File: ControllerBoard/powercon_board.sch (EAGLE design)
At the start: 49 parts, among them CN1 POWER_IF, CN2 PICkit_IF, CN3 ROTARY_ENCODER, CN4 UART_IF, CN5 POWER_IF_FOR_ESP, Q1 2SC1815, SW1 10-XX, SW2 10-XX, SW3 10-XX, SW4 10-XX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

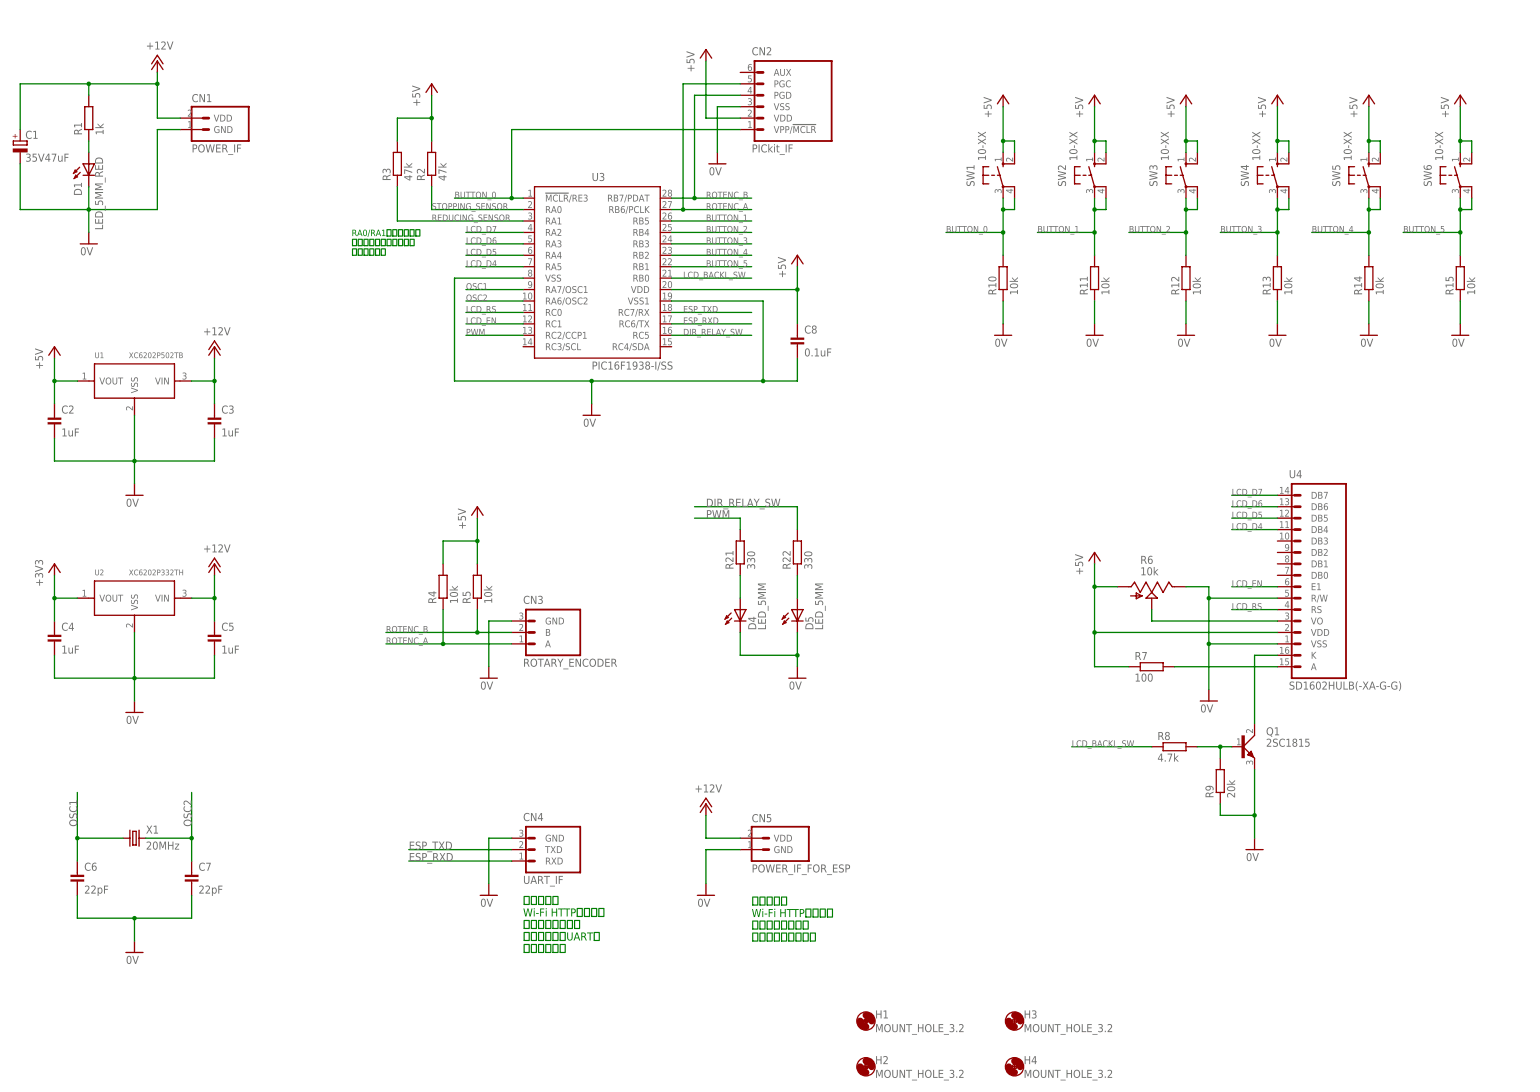
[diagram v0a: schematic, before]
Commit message: MODE_SELECT端子を新設
・PICのファームウェアを共通化する目的
・MODE_SELECT=LOWの場合は親機（パワーコントローラー部）
・MODE_SELECT=HIGHの場合は子機（リモコン部）
・ディレクトリー名を EAGLE —> ControllerBoardに改称
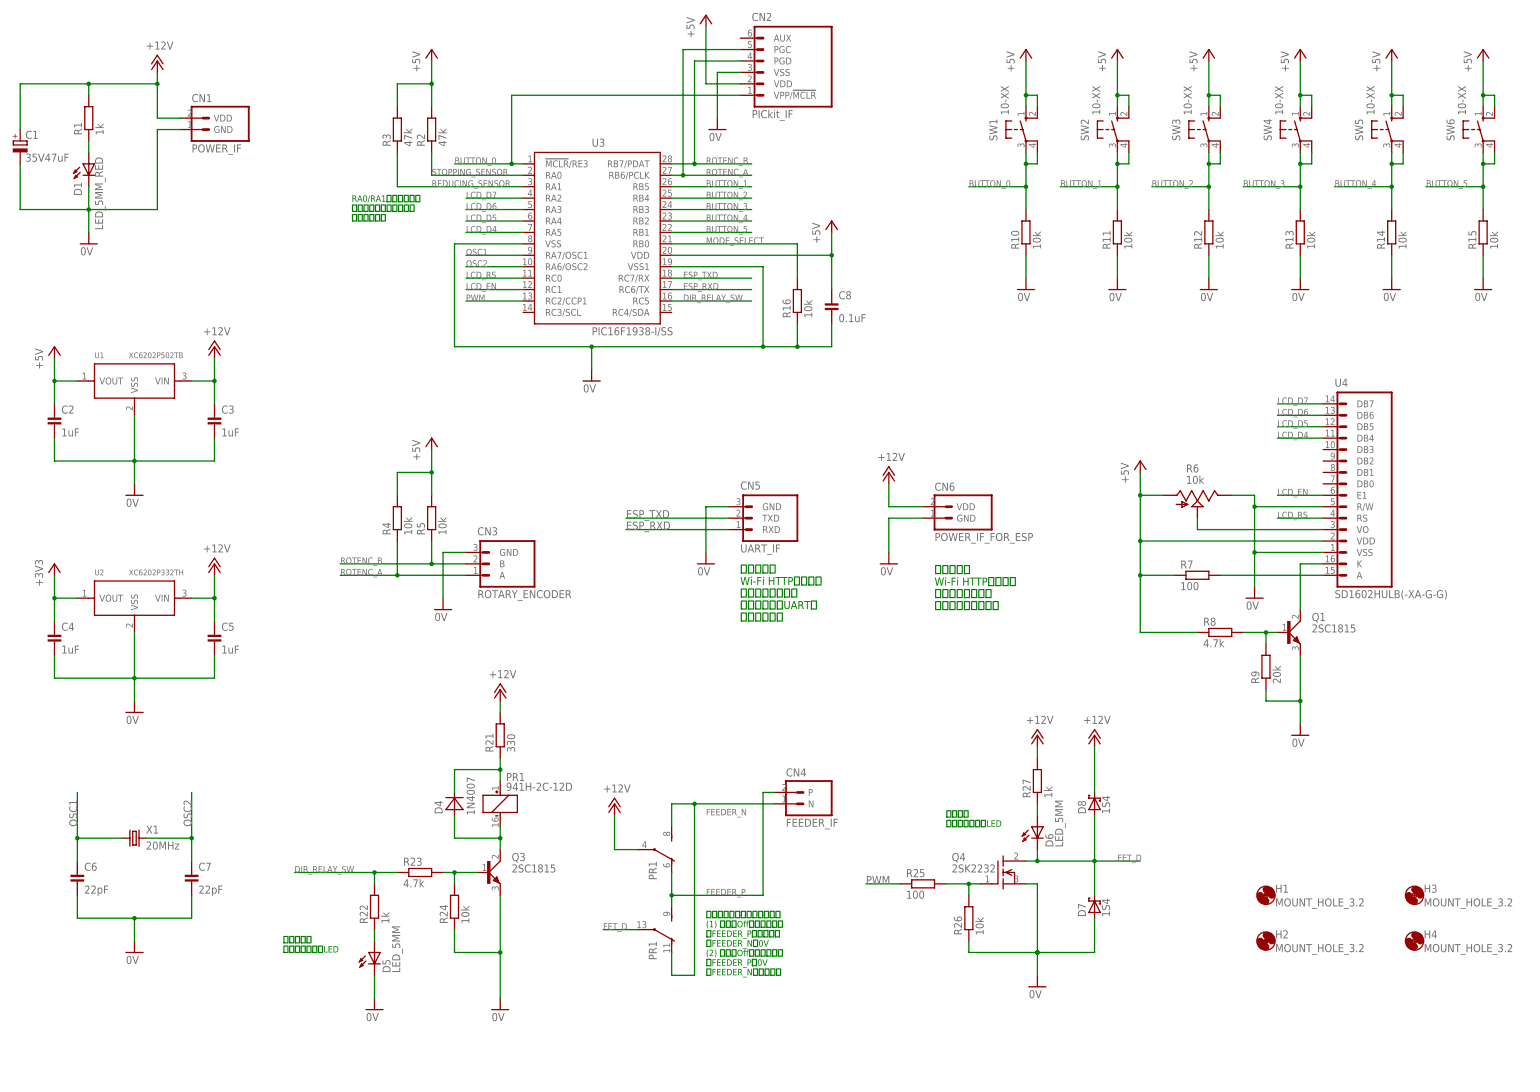
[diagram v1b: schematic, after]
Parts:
- added CN6: POWER_IF_FOR_ESP, PartsForProto:POWER_IF
- added D6: LED_5MM, Parts:LED_5MM
- added D7, D8: 1S4, Parts:1S4
- added PR1: 941H-2C-12D, Parts:941H-2C-12D
- added Q3: 2SC1815, Parts:2SC1815
- added Q4: 2SK2232, Parts:2SK2232
- added R16, R24, R26: 10k, Parts:RESISTOR_300MIL
- added R23: 4.7k, Parts:RESISTOR_300MIL
- added R25: 100, Parts:RESISTOR_300MIL
- added R27: 1k, Parts:RESISTOR_300MIL
- CN4: value UART_IF -> FEEDER_IF; device PartsForProto:UART_IF -> PartsForProto:FEEDER_IF
- CN5: value POWER_IF_FOR_ESP -> UART_IF; device PartsForProto:POWER_IF -> PartsForProto:UART_IF
- D4: value LED_5MM -> 1N4007; device Parts:LED_5MM -> Parts:1N4007
- R22: value 330 -> 1k
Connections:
- removed net LCD_BACKL_SW: R8.1, U3.RB0
- new net +3V3: C4.1, U2.VOUT
- new net FEEDER_N: CN4.N, PR12.S, PR13.O
- new net FEEDER_P: CN4.P, PR12.O, PR13.S
- new net FET_D: D6.C, D7.C, D8.A, PR13.P, Q4.D
- new net MODE_SELECT: R16.2, U3.RB0
- new net N$13: D4.C, PR11.+, R21.1
- new net N$14: Q3.B, R23.2, R24.2
- new net N$15: D4.A, PR11.-, Q3.C
- new net N$3: Q4.G, R25.2, R26.2
- net +12V: now also CN6.VDD, D8.C, PR12.P, R21.2, R27.2; no longer CN5.VDD
- net +5V: now also R8.1; no longer C4.1, U2.VOUT
- net 0V: now also CN6.GND, D7.A, Q3.E, Q4.S, R16.1, R24.1, R26.1; no longer CN4.GND, D4.C
- net DIR_RELAY_SW: now also R23.1
- net ESP_RXD: now also CN5.RXD; no longer CN4.RXD
- net ESP_TXD: now also CN5.TXD; no longer CN4.TXD
- net N$8: now also D6.A, R27.1; no longer D4.A, R21.1
- net PWM: now also R25.1; no longer R21.2
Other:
- note added: "フィーダーの正転／逆転制御 (1) リレーOff時（正転時） FEEDER_P：駆動電圧 FEEDER_N：0V (2) リレーOff時（逆転時） FEEDER_P：0V FEEDER_N：駆動電圧"
- note added: "供給電圧 インジケーターLED"
- note added: "別途作成の Wi-Fi HTTP通信基板 （親機モード）の ソフトウェアUARTに 接続します。"
- note added: "別途作成の Wi-Fi HTTP通信基板 （親機モード）へ 電源を供給します。"
- note added: "正転／逆転 インジケーターLED"
- note removed: "別途作成の Wi-Fi HTTP通信基板 （子機モード）の ソフトウェアUARTに 接続します。"
- note removed: "別途作成の Wi-Fi HTTP通信基板 （子機モード）へ 電源を供給します。"
- moved on the sheet: C8, CN2, CN3, D5, H1, H2, H3, H4, Q1, R10, R11, R12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
